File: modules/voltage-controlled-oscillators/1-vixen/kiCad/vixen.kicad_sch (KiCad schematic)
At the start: 72 parts, among them J1 PWR, J2 1V/OCT, J3 FM, J4 PWM, J5 PULSE, J6 SAW, Q1 BC558, Q2 BC548, U1 TL074, U2 40106

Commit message: update pcbs and symbols
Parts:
- added J7: Conn_01x03, Connector_PinHeader_2.54mm:PinHeader_1x03_P2.54mm_Vertical, symbol Connector_Generic:Conn_01x03
- added TP8: PULSE_OUT, Connector_Pin:Pin_D1.0mm_L10.0mm, symbol Connector:TestPoint
- C7: footprint synth-custom:C_RECT_WIMA_0.1uF -> Synth:C_RECT_WIMA_0.1uF
- C9: footprint synth-custom:C_RECT_MKT_1uF -> Synth:C_RECT_MKT_1uF
- D1, D2: footprint Diode_THT:D_DO-41_SOD81_P10.16mm_Horizontal -> Synth:D_DO-41_SOD81_P10.16mm_Horizontal; symbol Diode:1N5819 -> synth:D_Schottky (1N5819)
- D3: footprint synth-custom:D_default -> Synth:D_DO-35_SOD27_P7.62mm_Horizontal; symbol Diode:1N4148 -> synth:D_Signal (1N4148)
- H1, H12: footprint synth-custom:PinHeader_1x08_P2.54mm_Vertical -> Synth:PinHeader_1x08_P2.54mm_Vertical; symbol Synth_Custom:CONN_Header_01x08 -> synth:PinHeader_01x08
- H11, H2: footprint synth-custom:PinSocket_1x08_P2.54mm_Vertical -> Synth:PinSocket_1x08_P2.54mm_Vertical; symbol Synth_Custom:CONN_Socket_01x08 -> synth:PinSocket_01x08
- J1: footprint synth-custom:CONN_02x08_PWR -> Synth:IDC-Header_2x08_P2.54mm_Vertical; symbol Synth_Custom:CONN_02x08_PWR_Eurorack -> synth:Conn_02x08_EuroRack_Power
- J2, J3, J4, J5, J6: footprint synth-custom:Jack_default -> Connector_Audio:Jack_3.5mm_QingPu_WQP-PJ398SM_Vertical_CircularHoles; symbol Synth_Custom:Jack_default -> synth:AudioJack_Mono_3.5mm
- R1, R10, R11, R12, R13, R14, R15, R16, R17, R18, R19, R2, R20, R21, R3, R4, R5, R6, R7, R8, R9: footprint synth-custom:R_default -> Synth:R_Default (DIN0207); symbol Device:R -> synth:R_Default
- TP1: value D -> GND
- TP2: value D -> -12V
- TP3: value D -> +12V
- TP4: value A -> IN_CV
- TP5: value B -> CNTL_CV
- TP6: value C -> SAW_OUT
- TP7: value D -> PWM_CTRL
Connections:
- net +12V: now also R1.2, R11.1, R3.1; no longer R1.1, R11.2, R3.2
- net -12V: now also R2.2, R4.2, R5.2; no longer R2.1, R4.1, R5.1
- net GNDREF: now also R12.2, R14.1, R17.2, R18.1, J7.1 (Pin_1); no longer R12.1, R14.2, R17.1, R18.2
- net at H2.1 (Pin_3), Q1.2 (B): now also R10.2; no longer R10.1
- net at COURSE1.1: now also R3.2; no longer R3.1
- net at RV1.1, RV1.2: now also R10.1; no longer R10.2
- net at R9.1: now also VR4.1; no longer J3.T
- net at R9.2: now also J3.T; no longer VR4.1
- net at R16.1: now also R18.2, U1.12 (+); no longer U1.8
- net at C9.2, TP6.1, U1.10 (+)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: now also R12.1; no longer R12.2
- net at D2.2 (A): now also R2.1; no longer R2.2
- net at H2.3 (Pin_3): now also J7.2 (Pin_2)
- net at COURSE1.2: now also R6.2; no longer R6.1
- net at COURSE1.3: now also R4.1; no longer R4.2
- net at R20.1: now also J5.T; no longer H1.8
- net at R20.2: now also H1.8 (Pin_8); no longer J5.T
- net at VR2.1: now also R7.1; no longer R7.2
- net at Q1.3 (E), Q2.2 (B), TP4.1: now also R11.2; no longer R11.1
- net at D1.1 (K): now also R1.1; no longer R1.2
- net at H2.7 (Pin_7), U1.7: now also R19.2; no longer R19.1
- net at R8.1: now also VR3.1; no longer J2.T
- net at R8.2: now also J2.T; no longer VR3.1
- net at FINE1.2: now also R7.2; no longer R7.1
- net at PWM_CNTR1.2, PWM_CNTR1.3: now also R13.1; no longer R13.2
- net at VR1.1: now also R6.1; no longer R6.2
- net at H2.8 (Pin_8), U1.13 (-), U1.14: now also TP8.1
- net at R15.2: now also H1.2 (Pin_2), R13.2, R14.2, TP7.1; no longer PWM_AMT1.2
- net at J6.T: now also R21.2; no longer R21.1
- net at H1.7 (Pin_7): now also R21.1; no longer R21.2
- net at FINE1.3: now also R5.1; no longer R5.2
- net at J2.TN: now also H1.3 (Pin_3)
- net at J1.13 (CV): now also J1.14 (CV), J7.3 (Pin_3)
- new net: R17.1, R19.1, U1.6 (-)
- new net: R16.2, U1.8
- new net: PWM_AMT1.2, R15.1
- no-connect marks 32 -> 27
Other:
- moved on the sheet: C1, C5, C6, C8, C9, COURSE1, FINE1, J2, J3, J4, J5, J6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

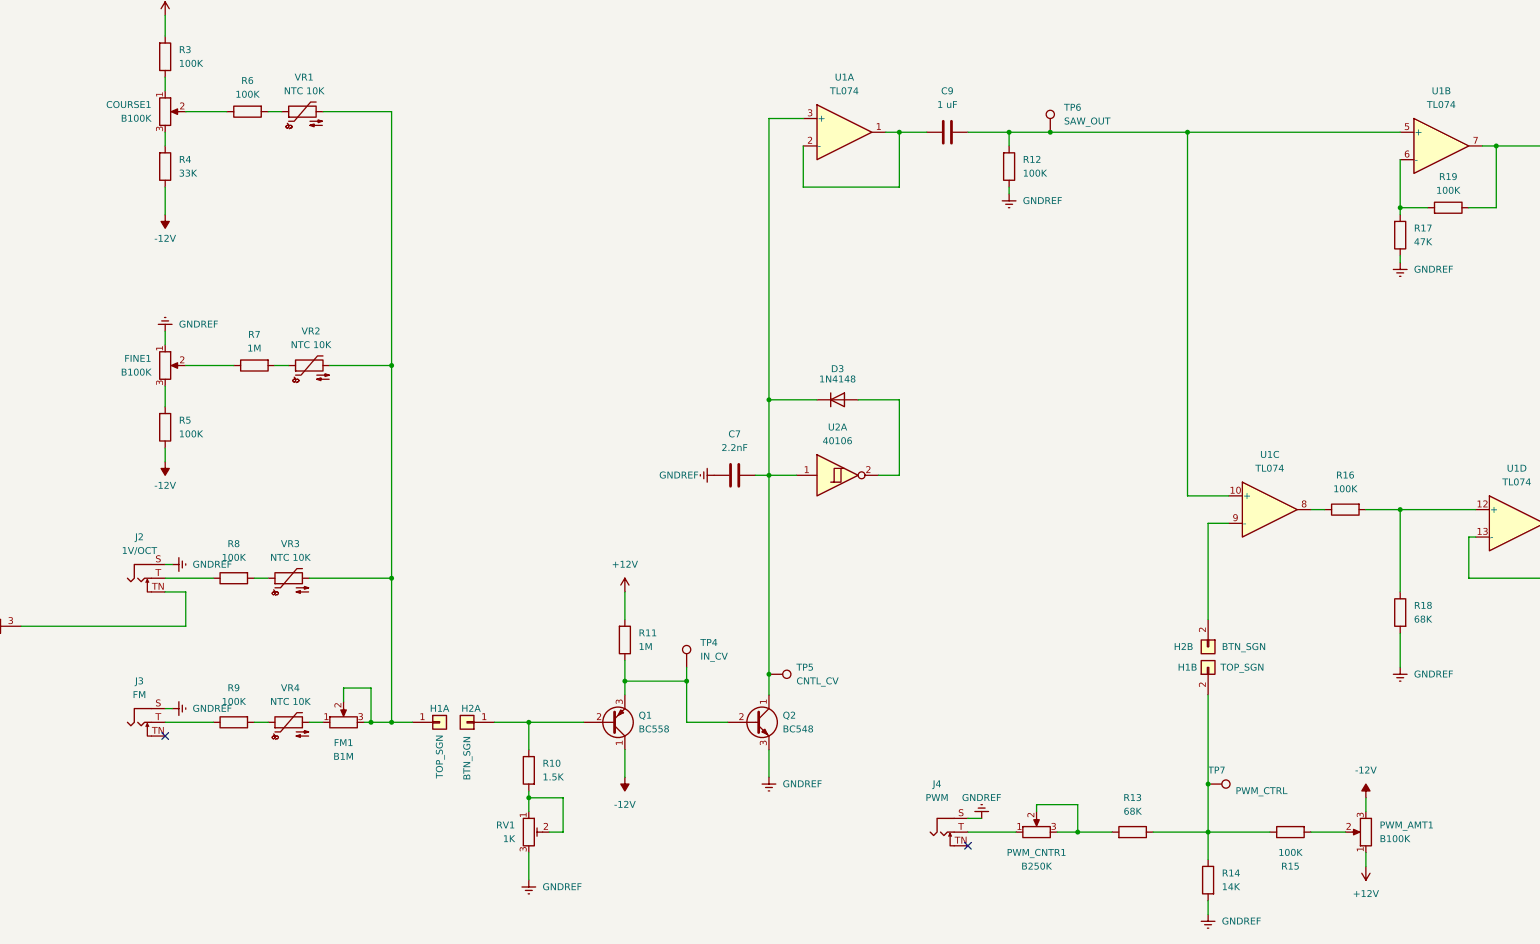
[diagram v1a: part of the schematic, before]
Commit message: add images and finish Vixen VCO schematics and pcb
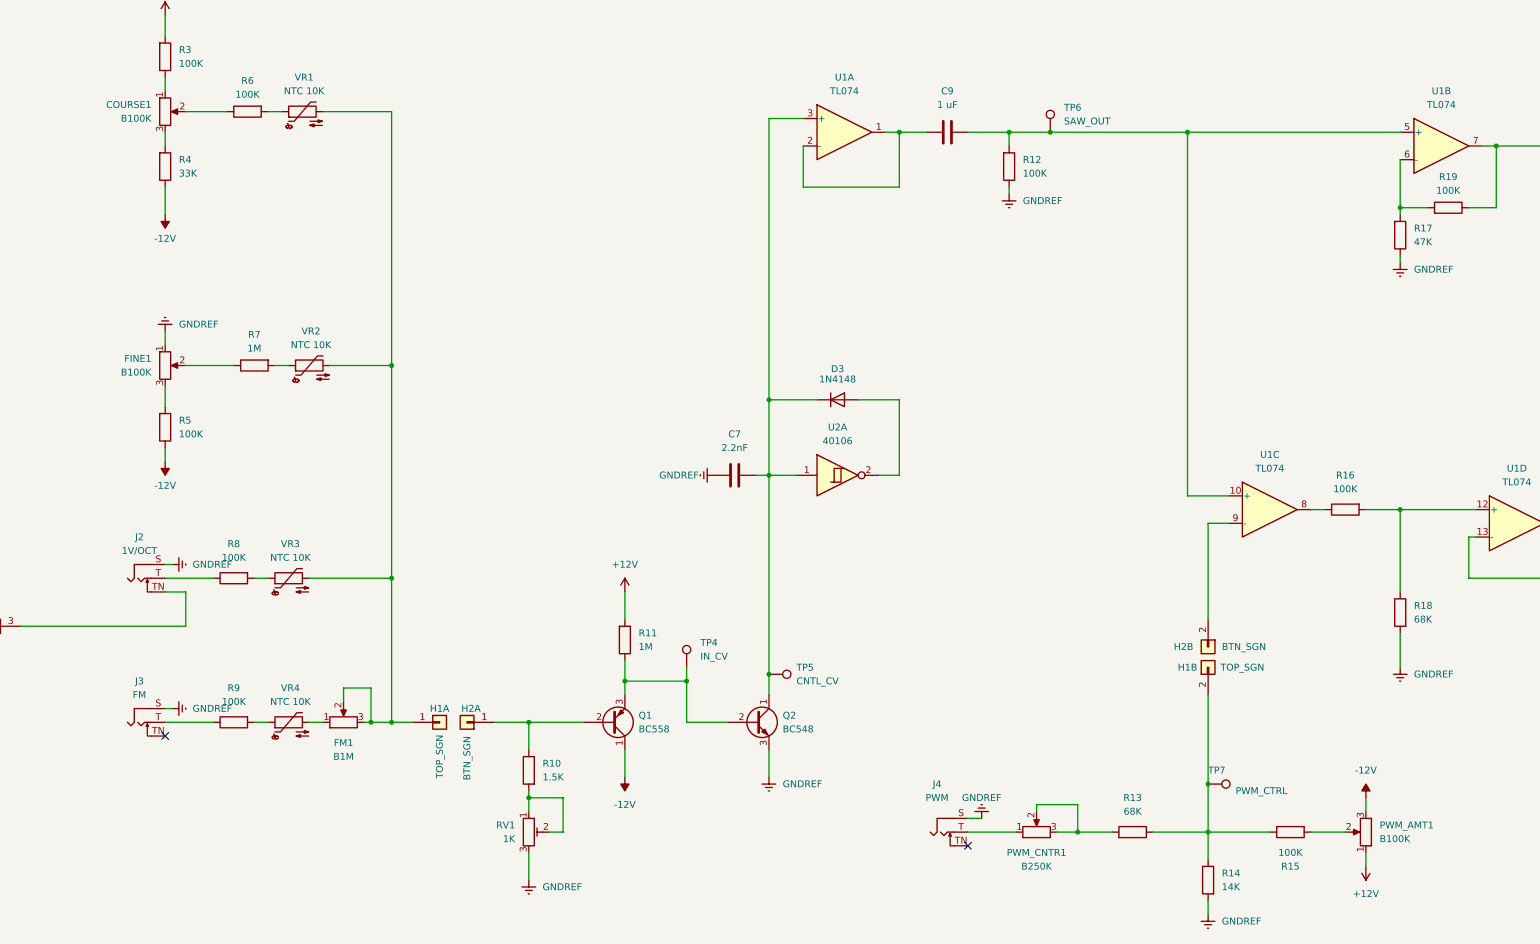
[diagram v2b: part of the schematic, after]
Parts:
- C7: symbol Device:C -> synth:C_sm (MKS)
- C9: symbol Device:C -> synth:C_1uF (MKS)
- COURSE1, FINE1, FM1, PWM_AMT1: footprint Potentiometer_THT:Potentiometer_TT_P0915N -> Synth:Potentiometer_TT_P0915N; symbol Device:R_Potentiometer -> synth:R_Potentiometer (P0915N)
- J2, J3, J4, J5, J6: footprint Connector_Audio:Jack_3.5mm_QingPu_WQP-PJ398SM_Vertical_CircularHoles -> Synth:Jack_3.5mm_QingPu_WQP-PJ398SM_Vertical_CircularHoles
- PWM_CNTR1: footprint Potentiometer_THT:Potentiometer_TT_P0915N -> Synth:Potentiometer_Alpha_RD901F-40-00D_Single_Vertical_CircularHoles; symbol Device:R_Potentiometer -> synth:R_Potentiometer (Alpha_9mm)
- Q1, Q2: footprint Package_TO_SOT_THT:TO-92_HandSolder -> Package_TO_SOT_THT:TO-92_Inline
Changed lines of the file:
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@@
 	)
 	(symbol
-		(lib_id "Device:R_Potentiometer")
+		(lib_id "synth:R_Potentiometer (P0915N)")
 		(at 73.66 40.64 0)
 		(unit 1)
@@
 		(fields_autoplaced yes)
 		(property "Reference" "COURSE1"
-			(at 71.12 39.37 0)
+			(at 71.12 39.3699 0)
 			(effects
 				(font
@@
 		)
 		(property "Value" "B100K"
-			(at 71.12 41.91 0)
+			(at 71.12 41.9099 0)
 			(effects
 				(font
@@
 			)
 		)
-		(property "Footprint" "Potentiometer_THT:Potentiometer_TT_P0915N"
-			(at 73.66 40.64 0)
+		(property "Footprint" "Synth:Potentiometer_TT_P0915N"
+			(at 73.66 54.356 0)
 			(effects
 				(font
@@
 		)
 		(property "Datasheet" "~"
-			(at 73.66 40.64 0)
+			(at 73.66 51.308 0)
 			(effects
 				(font
@@
 		)
 		(property "Description" "Potentiometer"
-			(at 73.66 40.64 0)
+			(at 73.66 52.578 0)
 			(effects
 				(font
@@
 			)
 		)
-		(property "Footprint" "Package_TO_SOT_THT:TO-92_HandSolder"
+		(property "Footprint" "Package_TO_SOT_THT:TO-92_Inline"
 			(at 187.96 155.575 0)
 			(effects
@@
 	)
 	(symbol
-		(lib_id "Device:C")
+		(lib_id "synth:C_sm (MKS)")
 		(at 179.07 107.95 270)
 		(unit 1)
@@
 		)
 		(property "Footprint" "Synth:C_RECT_WIMA_0.1uF"
-			(at 175.26 108.9152 0)
+			(at 165.608 108.966 0)
 			(effects
 				(font
@@
 		)
 		(property "Description" "Unpolarized capacitor"
-			(at 179.07 107.95 0)
+			(at 167.64 107.696 0)
 			(effects
 				(font
@@
 	)
 	(symbol
-		(lib_id "Device:R_Potentiometer")
+		(lib_id "synth:R_Potentiometer (Alpha_9mm)")
 		(at 234.95 173.99 90)
 		(unit 1)
@@
 			)
 		)
-		(property "Footprint" "Potentiometer_THT:Potentiometer_TT_P0915N"
-			(at 234.95 173.99 0)
+		(property "Footprint" "Synth:Potentiometer_Alpha_RD901F-40-00D_Single_Vertical_CircularHoles"
+			(at 248.92 173.99 0)
 			(effects
 				(font
@@
 		)
 		(property "Datasheet" "~"
-			(at 234.95 173.99 0)
+			(at 245.618 173.99 0)
 			(effects
 				(font
@@
 		)
 		(property "Description" "Potentiometer"
-			(at 234.95 173.99 0)
+			(at 246.888 173.99 0)
 			(effects
 				(font
@@
 			)
 		)
-		(property "Footprint" "Connector_Audio:Jack_3.5mm_QingPu_WQP-PJ398SM_Vertical_CircularHoles"
+		(property "Footprint" "Synth:Jack_3.5mm_QingPu_WQP-PJ398SM_Vertical_CircularHoles"
 			(at 217.17 178.562 0)
 			(effects
@@
 	)
 	(symbol
-		(lib_id "Device:R_Potentiometer")
+		(lib_id "synth:R_Potentiometer (P0915N)")
 		(at 295.91 173.99 180)
 		(unit 1)
@@
 		(fields_autoplaced yes)
 		(property "Reference" "PWM_AMT1"
-			(at 298.45 172.72 0)
+			(at 298.45 172.7199 0)
 			(effects
 				(font
@@
 		)
 		(property "Value" "B100K"
-			(at 298.45 175.26 0)
+			(at 298.45 175.2599 0)
 			(effects
 				(font
@@
 			)
 		)
-		(property "Footprint" "Potentiometer_THT:Potentiometer_TT_P0915N"
-			(at 295.91 173.99 0)
+		(property "Footprint" "Synth:Potentiometer_TT_P0915N"
+			(at 295.91 160.274 0)
 			(effects
 				(font
@@
 		)
 		(property "Datasheet" "~"
-			(at 295.91 173.99 0)
+			(at 295.91 163.322 0)
 			(effects
 				(font
@@
 		)
 		(property "Description" "Potentiometer"
-			(at 295.91 173.99 0)
+			(at 295.91 162.052 0)
 			(effects
 				(font
@@
 			)
 		)
-		(property "Footprint" "Connector_Audio:Jack_3.5mm_QingPu_WQP-PJ398SM_Vertical_CircularHoles"
+		(property "Footprint" "Synth:Jack_3.5mm_QingPu_WQP-PJ398SM_Vertical_CircularHoles"
 			(at 387.35 42.418 0)
 			(effects
@@
 			)
 		)
-		(property "Footprint" "Package_TO_SOT_THT:TO-92_HandSolder"
+		(property "Footprint" "Package_TO_SOT_THT:TO-92_Inline"
 			(at 161.29 151.765 0)
 			(effects
@@
 			)
 		)
-		(property "Footprint" "Connector_Audio:Jack_3.5mm_QingPu_WQP-PJ398SM_Vertical_CircularHoles"
+		(property "Footprint" "Synth:Jack_3.5mm_QingPu_WQP-PJ398SM_Vertical_CircularHoles"
 			(at 68.58 158.242 0)
 			(effects
@@
 	)
 	(symbol
-		(lib_id "Device:R_Potentiometer")
+		(lib_id "synth:R_Potentiometer (P0915N)")
 		(at 73.66 87.63 0)
 		(unit 1)
@@
 		(fields_autoplaced yes)
 		(property "Reference" "FINE1"
-			(at 71.12 86.36 0)
+			(at 71.12 86.3599 0)
 			(effects
 				(font
@@
 		)
 		(property "Value" "B100K"
-			(at 71.12 88.9 0)
+			(at 71.12 88.8999 0)
 			(effects
 				(font
@@
 			)
 		)
-		(property "Footprint" "Potentiometer_THT:Potentiometer_TT_P0915N"
-			(at 73.66 87.63 0)
+		(property "Footprint" "Synth:Potentiometer_TT_P0915N"
+			(at 73.66 101.346 0)
 			(effects
 				(font
@@
 		)
 		(property "Datasheet" "~"
-			(at 73.66 87.63 0)
+			(at 73.66 98.298 0)
 			(effects
 				(font
@@
 		)
 		(property "Description" "Potentiometer"
-			(at 73.66 87.63 0)
+			(at 73.66 99.568 0)
 			(effects
 				(font
@@
 			)
 		)
-		(property "Footprint" "Connector_Audio:Jack_3.5mm_QingPu_WQP-PJ398SM_Vertical_CircularHoles"
+		(property "Footprint" "Synth:Jack_3.5mm_QingPu_WQP-PJ398SM_Vertical_CircularHoles"
 			(at 68.58 131.572 0)
 			(effects
@@
 	)
 	(symbol
-		(lib_id "Device:C")
+		(lib_id "synth:C_1uF (MKS)")
 		(at 218.44 44.45 90)
 		(unit 1)
@@
 		)
 		(property "Footprint" "Synth:C_RECT_MKT_1uF"
-			(at 222.25 43.4848 0)
+			(at 231.648 43.942 0)
 			(effects
 				(font
@@
 		)
 		(property "Description" "Unpolarized capacitor"
-			(at 218.44 44.45 0)
+			(at 229.616 44.45 0)
 			(effects
 				(font
@@
 			)
 		)
-		(property "Footprint" "Connector_Audio:Jack_3.5mm_QingPu_WQP-PJ398SM_Vertical_CircularHoles"
+		(property "Footprint" "Synth:Jack_3.5mm_QingPu_WQP-PJ398SM_Vertical_CircularHoles"
 			(at 386.08 112.268 0)
 			(effects
@@
 	)
 	(symbol
-		(lib_id "Device:R_Potentiometer")
+		(lib_id "synth:R_Potentiometer (P0915N)")
 		(at 106.68 153.67 90)
 		(unit 1)
@@
 			)
 		)
-		(property "Footprint" "Potentiometer_THT:Potentiometer_TT_P0915N"
-			(at 106.68 153.67 0)
+		(property "Footprint" "Synth:Potentiometer_TT_P0915N"
+			(at 120.396 153.67 0)
 			(effects
 				(font
@@
 		)
 		(property "Datasheet" "~"
-			(at 106.68 153.67 0)
+			(at 117.348 153.67 0)
 			(effects
 				(font
@@
 		)
 		(property "Description" "Potentiometer"
-			(at 106.68 153.67 0)
+			(at 118.618 153.67 0)
 			(effects
 				(font

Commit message: add gerber files and ZIPs for V2
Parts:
- Q1, Q2: footprint Package_TO_SOT_THT:TO-92_Inline -> Package_TO_SOT_THT:TO-92_HandSolder
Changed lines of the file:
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@@
 			)
 		)
-		(property "Footprint" "Package_TO_SOT_THT:TO-92_Inline"
+		(property "Footprint" "Package_TO_SOT_THT:TO-92_HandSolder"
 			(at 187.96 155.575 0)
 			(effects
@@
 			)
 		)
-		(property "Footprint" "Package_TO_SOT_THT:TO-92_Inline"
+		(property "Footprint" "Package_TO_SOT_THT:TO-92_HandSolder"
 			(at 161.29 151.765 0)
 			(effects

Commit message: 7555 readme
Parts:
- C5, C6, C8: value 0.1uF -> 100nF; footprint Capacitor_THT:CP_Radial_D4.0mm_P2.00mm -> Synth:C_RECT_WIMA_0.1uF; symbol Device:C_Polarized -> Device:C
- C9: value 1 uF -> 1uF
- H1: value TOP_SGN -> Conn_01x08
- H10, H3, H4, H5, H6, H7, H8, H9, TP1, TP2, TP3, TP4, TP5, TP6, TP7, TP8: now left out of the parts list
- H11: value BTM_PWR -> Conn_01x08
- H12: value TOP_PWR -> Conn_01x08
- H2: value BTN_SGN -> Conn_01x08
- R1, R2: value 10 -> 10R
- R10: value 1.5K -> 1K5

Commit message: quantizers_stls
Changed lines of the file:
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@@
 (kicad_sch
-	(version 20231120)
+	(version 20250114)
 	(generator "eeschema")
-	(generator_version "8.0")
+	(generator_version "9.0")
 	(paper "A3")
+	(rectangle
+		(start 17.78 233.045)
+		(end 136.525 278.765)
+		(stroke
+			(width 0)
+			(type default)
+		)
+		(fill
+			(type none)
+		)
+	)
+	(rectangle
+		(start 300.355 203.2)
+		(end 407.035 252.095)
+		(stroke
+			(width 0)
+			(type default)
+		)
+		(fill
+			(type none)
+		)
+	)
+	(rectangle
+		(start 229.87 233.045)
+		(end 280.035 278.13)
+		(stroke
+			(width 0)
+			(type default)
+		)
+		(fill
+			(type none)
+		)
+	)
+	(rectangle
+		(start 180.34 233.045)
+		(end 229.87 278.13)
+		(stroke
+			(width 0)
+			(type default)
+		)
+		(fill
+			(type none)
+		)
+	)
+	(rectangle
+		(start 136.525 233.045)
+		(end 180.34 278.13)
+		(stroke
+			(width 0)
+			(type default)
+		)
+		(fill
+			(type none)
+		)
+	)
 	(junction
 		(at 140.97 153.67)
@@
 		)
 	)
-	(rectangle
-		(start 17.78 233.045)
-		(end 136.525 278.765)
-		(stroke
-			(width 0)
-			(type default)
-		)
-		(fill
-			(type none)
-		)
-	)
-	(rectangle
-		(start 300.355 203.2)
-		(end 407.035 252.095)
-		(stroke
-			(width 0)
-			(type default)
-		)
-		(fill
-			(type none)
-		)
-	)
-	(rectangle
-		(start 229.87 233.045)
-		(end 280.035 278.13)
-		(stroke
-			(width 0)
-			(type default)
-		)
-		(fill
-			(type none)
-		)
-	)
-	(rectangle
-		(start 180.34 233.045)
-		(end 229.87 278.13)
-		(stroke
-			(width 0)
-			(type default)
-		)
-		(fill
-			(type none)
-		)
-	)
-	(rectangle
-		(start 136.525 233.045)
-		(end 180.34 278.13)
-		(stroke
-			(width 0)
-			(type default)
-		)
-		(fill
-			(type none)
-		)
-	)
 	(symbol
 		(lib_id "power:GNDREF")
@@
 		)
 	)
+	(embedded_fonts no)
 )
